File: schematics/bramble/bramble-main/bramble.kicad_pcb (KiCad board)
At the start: 2 copper layers, 50.1 x 72.3 mm, 74 parts, among them IC1 RP2040_QFN56, J1 Conn_01x05_Pin, J2 Conn_01x03, J3 USB_C_Receptacle_USB2.0_16P, J5 U.FL, J6 Conn_01x03_Pin, J7 Conn_02x06_Odd_Even, Q1 DMN3300U, SW1 STM_RESET, SW2 BOOT, SW4 RESET, U1 TDN_5-0910WISM, U2 Opamp_Quad, U3 STM32L031F6P6TR, U4 RFM95W-915S2, U5 MCP1700x-120xxMB, U6 MT25QL01GBBB8ESF-0SIT, U7 W25Q16JVSS, Y1 Crystal, Y3 Crystal

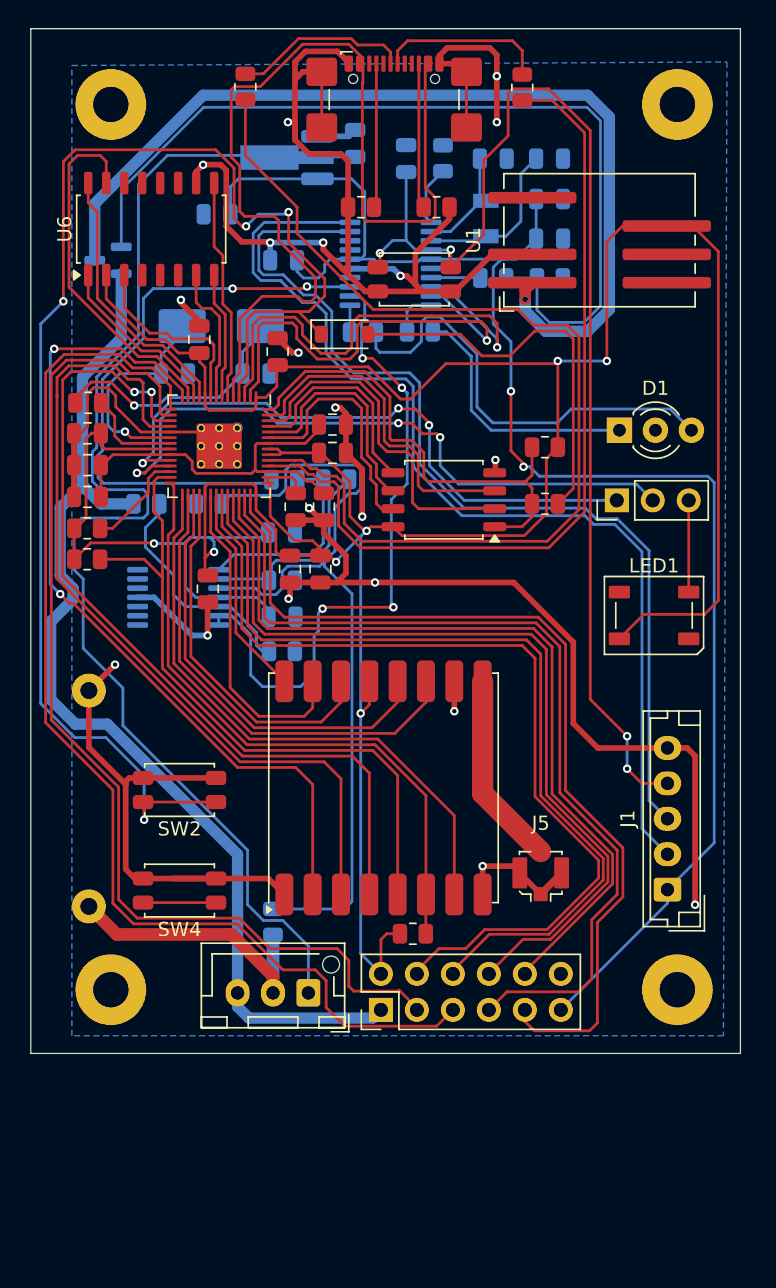
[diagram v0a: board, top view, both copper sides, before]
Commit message: fix: swap spi pins, change footprints, etc
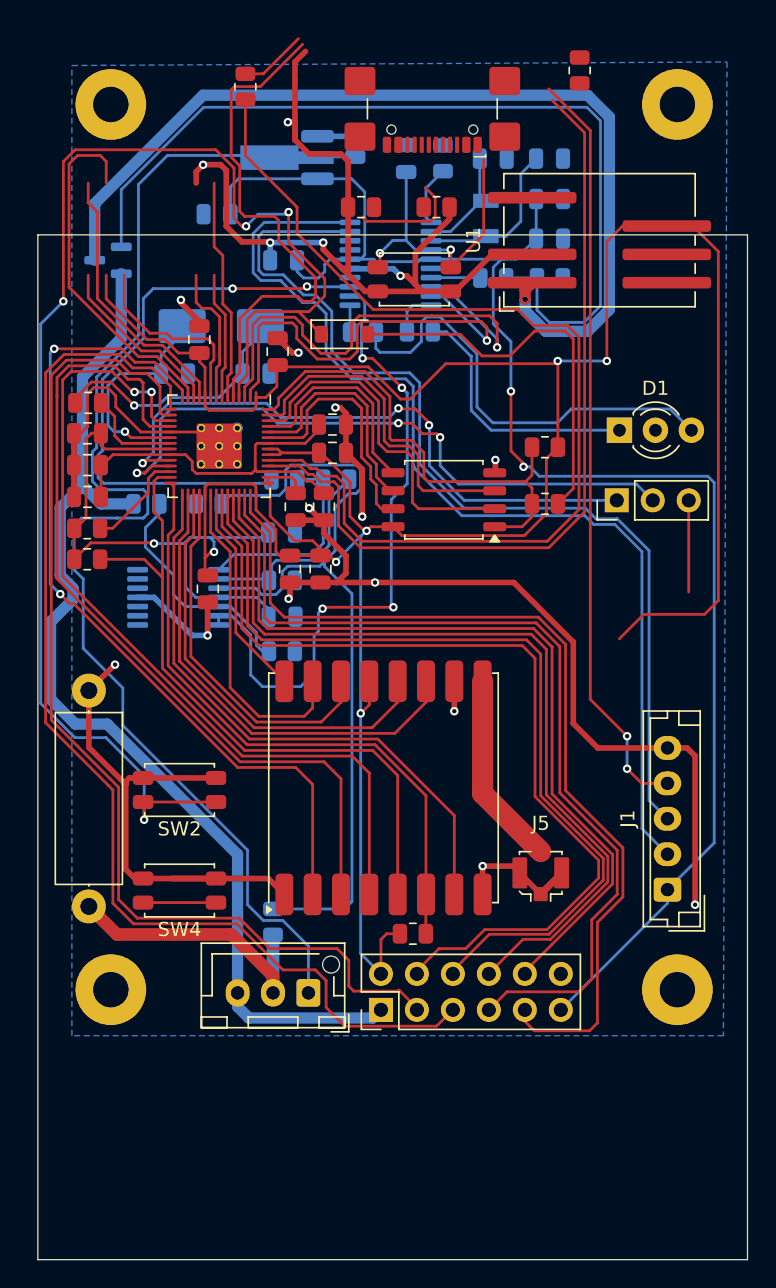
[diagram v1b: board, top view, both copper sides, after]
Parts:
- removed LED1: WS2812B_SK6805_1515, LED_SMD:LED_WS2812B_PLCC4_5.0x5.0mm_P3.2mm
- removed U6: MT25QL01GBBB8ESF-0SIT, Package_SO:SOP-16_4.55x10.3mm_P1.27mm
- R6: moved to F.Cu
- moved R18 4.22 mm to (49.9, 14.6)
- moved J3 3.15 mm to (39.5, 16.2), turned to 180 degrees
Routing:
- net GND: track 249.7 -> 224.8 mm, vias 20 -> 18
- net VBUS: track 69.2 -> 44.5 mm
- net Net-(J3-D--PadA7): track 12.0 -> 0.00 mm
- net Net-(J3-CC1): track 10.2 -> 0.25 mm
- net Net-(J3-CC2): track 10.3 -> 0.48 mm
- net /pmu/NRST: track 83.3 -> 74.9 mm
- net Net-(J3-D+-PadA6): track 12.5 -> 4.78 mm
- net /rp2040/D+: track 59.5 -> 57.4 mm

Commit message: pre-fab check-in of v2
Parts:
- removed U1: TDN_5-0910WISM, Converter_DCDC:Converter_DCDC_TRACO_TDN_5-xxxxWISM_SMD
- added Q2: FDN360P, Package_TO_SOT_SMD:SOT-23, F.Cu at (53.5, 21.4)
- added R3: 100k, Capacitor_SMD:C_0805_2012Metric, F.Cu at (53.4, 26.9)
- added R4: 10k, Capacitor_SMD:C_0805_2012Metric, F.Cu at (53.4, 24.4)
- added RPI_STATUS: WS2812B_SK6805_1515, LED_SMD:LED_WS2812B-2020_PLCC4_2.0x2.0mm, F.Cu at (24.2, 16.8)
- added U7: MT25QL01GBBB8ESF-0SIT, Package_SO:SOIC-16W-12_7.5x10.3mm_P1.27mm, F.Cu at (19.1, 26.2)
- added VR1: TPSM861253RDXR, Bramble:VREG_TPSM861253RDXR, F.Cu at (58.0, 28.2)
- C10: renamed from C8; value 22pF -> 8pF
- C11: renamed from C9; value 22pF -> 8pF
- Q1, R1, R2: moved to F.Cu
- TPS_C_OUT1: renamed from C1; value 10uF -> 22uF
- moved Q1 37.1 mm to (53.2, 33.6), turned to -90 degrees
- moved R2 10.5 mm to (58.0, 31.6)
- moved R1 9.61 mm to (53.4, 29.6)
- moved R24 6.18 mm to (40.5, 23.2), turned to 90 degrees
- moved R21 4.79 mm to (31.0, 15.2)
- moved R23 2.30 mm to (37.7, 23.2), turned to 90 degrees
- moved C21 0.81 mm to (22.2, 33.7)
- renumbered SW2 to BOOT, C3 to C1, C10 to C12, C11 to C13, C12 to C14, C13 to C16, C14 to C17, C15 to C18, C16 to C19, C4 to C2, C17 to C20, C18 to C21, C19 to C22, C20 to C23, C5 to C3, C24 to C4, C23 to C5, C21 to C7, C22 to C8, C7 to C9, D3 to D2, J6 to J2, J2 to J3, J3 to J4, J7 to J6, J1 to PMU_DEBUG, D1 to PMU_STATUS, R8 to R10, R9 to R11, R10 to R12, R22 to R13, R23 to R14, R11 to R15, R12 to R16, R13 to R17, R14 to R18, R15 to R19, R16 to R20, R17 to R21, R18 to R22, R19 to R23, R20 to R24, R21 to R25, R3 to R5, R4 to R6, R5 to R7, R6 to R8, R7 to R9, SW4 to RESET, C2 to TPS_C_IN1, U5 to U4, U4 to U5, U7 to U6, Y3 to Y2
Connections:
- IC1 pad 11: /rp2040/MT25_SCK -> /rp2040/MISO
- IC1 pad 12: /rp2040/MT25_DQ3 -> unconnected-(IC1-GPIO9-Pad12)
- IC1 pad 13: /rp2040/MT25_DQ0 -> unconnected-(IC1-GPIO10-Pad13)
- IC1 pad 14: /rp2040/MISO -> unconnected-(IC1-GPIO11-Pad14)
- IC1 pad 54: /rp2040/QSPI_D1 -> /rp2040/QSPI_D2
- IC1 pad 55: /rp2040/QSPI_D2 -> /rp2040/QSPI_D1
- IC1 pad 6: /rp2040/MT25_DQ2 -> /rp2040/RGB_LED
- IC1 pad 7: /rp2040/MT25_DQ1 -> unconnected-(IC1-GPIO5-Pad7)
- Q1 pad 2: +9V -> GND
- RESET pad 1: unconnected-(SW4-Pad1) -> /rp2040/~{RESET}
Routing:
- net Net-(Q1-D): track 67.1 -> 8.21 mm, vias 1 -> 0
- net Net-(Q1-G): track 63.5 -> 6.18 mm
- net +9V: track 76.2 -> 131.8 mm, vias 0 -> 1
- net /pmu/3V3_POWER_ON: track 3.52 -> 43.1 mm, vias 0 -> 1
- net /rp2040/~{RESET}: track 7.21 -> 42.4 mm, vias 0 -> 2
- net GND: track 224.8 -> 259.2 mm, vias 18 -> 19
- net /rp2040/MT25_DQ0: track 25.3 -> 0.00 mm
- net /rp2040/RGB_LED: track 0.00 -> 23.9 mm
- net /rp2040/SCK: track 60.1 -> 80.4 mm, vias 2 -> 3
- net /rp2040/MT25_SCK: track 19.1 -> 0.00 mm
- net /rp2040/MOSI: track 59.9 -> 78.7 mm, vias 0 -> 2
- net /pmu/NRST: track 74.9 -> 93.2 mm, vias 4 -> 3
- net /rp2040/MISO: track 59.7 -> 76.8 mm
- net Net-(J4-D--PadA7): track 0.00 -> 16.7 mm, vias 0 -> 2
- net /rp2040/MT25_DQ2: track 15.7 -> 0.00 mm
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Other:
- board size 50.1 x 72.3 mm -> 50.4 x 70.7 mm
- board text added: "Bramble v0.2 Erik E. Beerepoot"
- board text added: "RPI_SWD"
- board text added: "⏚"

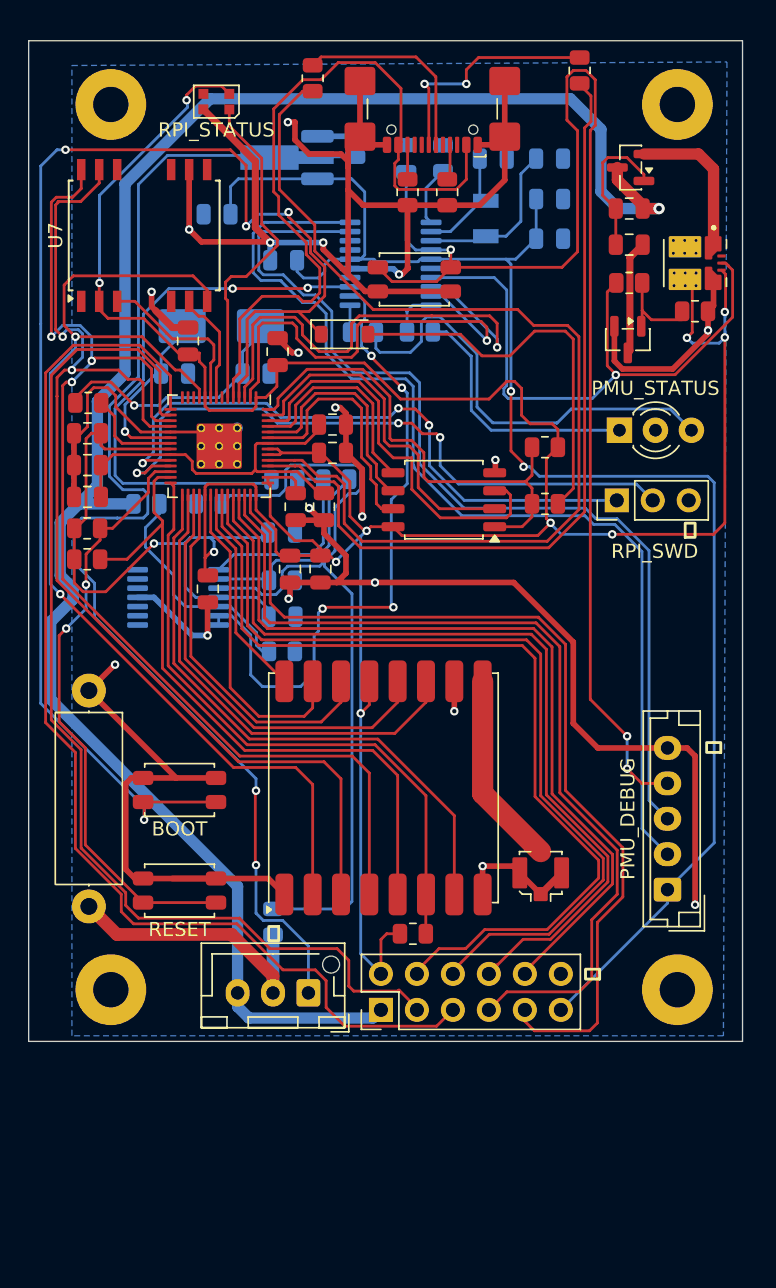
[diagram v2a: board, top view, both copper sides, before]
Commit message: v3: add art, reposition pin headers and ufl connector
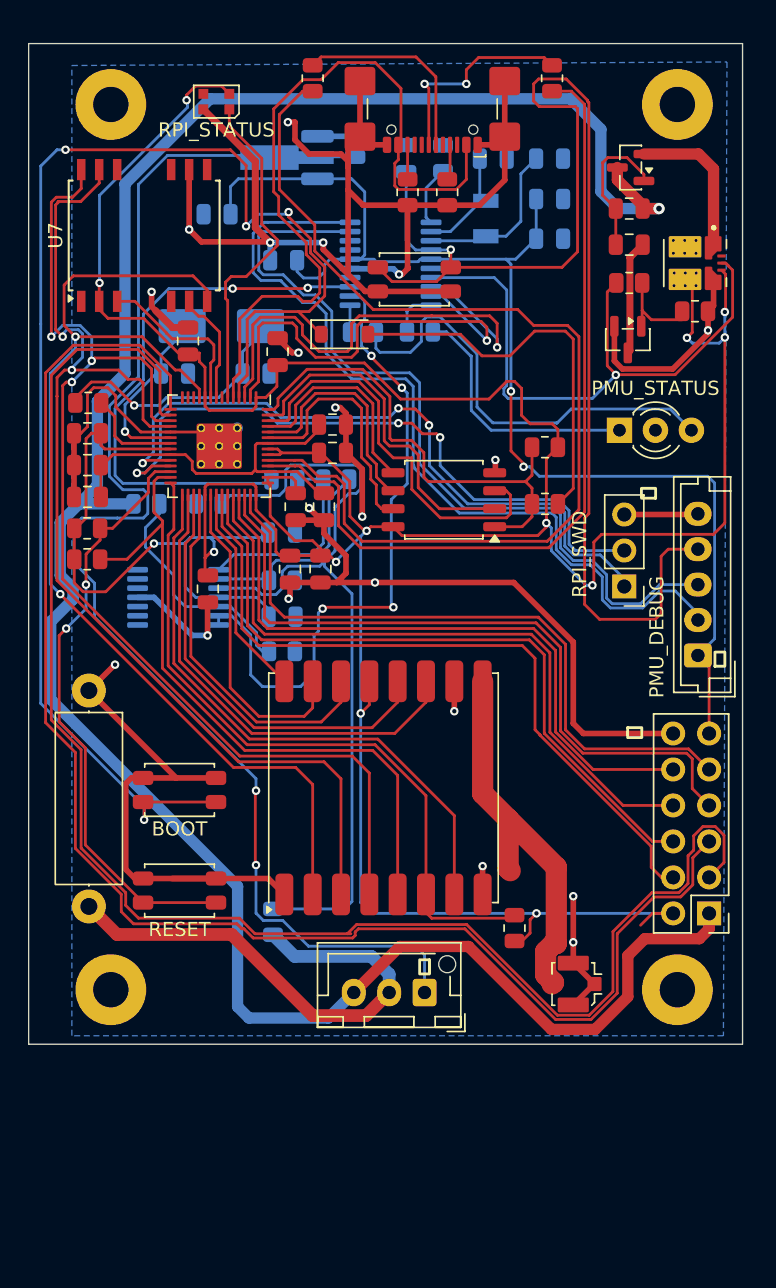
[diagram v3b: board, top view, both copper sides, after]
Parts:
- added G***: LOGO, Bramble:bramble logo, B.Cu at (44.9, 61.9)
- moved J6 24.2 mm to (59.0, 74.1), turned to 180 degrees
- moved PMU_DEBUG 16.7 mm to (58.2, 55.9)
- moved J2 8.20 mm to (38.9, 79.7)
- moved J5 8.18 mm to (49.4, 79.1), turned to -90 degrees
- moved R19 7.19 mm to (45.2, 75.2), turned to -90 degrees
- moved J3 6.10 mm to (53.0, 51.0), turned to 180 degrees
- moved R22 2.03 mm to (47.9, 15.2)
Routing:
- net /rp2040/VALVE_3: track 77.1 -> 112.0 mm
- net +9V: track 131.8 -> 165.0 mm
- net /rp2040/VALVE_4: track 81.5 -> 107.3 mm
- net +3V3: track 253.9 -> 277.9 mm, vias 12 -> 13
- net VDD: track 111.5 -> 88.3 mm
- net /rp2040/VALVE_1: track 66.7 -> 47.6 mm
- net /rp2040/VALVE_2: track 66.3 -> 50.8 mm
- net GNDPWR: track 20.3 -> 35.7 mm
- net Net-(J5-In): track 13.7 -> 27.9 mm
- net Net-(J1-Pin_2): track 72.7 -> 60.0 mm
- net /rp2040/MOTOR_HI_2: track 61.8 -> 49.4 mm
- net /rp2040/MOTOR_HI_1: track 63.9 -> 51.6 mm
- net /rp2040/MOTOR_LO_1: track 59.7 -> 47.9 mm
- net Net-(J1-Pin_3): track 69.2 -> 57.6 mm
- net /rp2040/MOTOR_LO_2: track 57.6 -> 46.4 mm
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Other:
- board size 50.4 x 70.7 mm -> 50.4 x 70.6 mm
- board text added: "BRAMBLE"
- board text added: "PWR"
- board text added: "v0.3 E. E. Beerepoot"
- board text removed: "Bramble v0.2 Erik E. Beerepoot"

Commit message: v3 of schematic
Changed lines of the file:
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@@
 	)
 	(segment
-		(start 47.85 48.502712)
-		(end 47.85 46.9)
-		(width 0.2)
-		(layer "B.Cu")
-		(net 7)
-	)
-	(segment
 		(start 19.796 48)
 		(end 21.93 48)
@@
 	)
 	(segment
-		(start 59.7 33.85)
-		(end 60.1 33.45)
+		(start 50.402 49.802)
+		(end 49.149288 49.802)
 		(width 0.2)
 		(layer "B.Cu")
@@
 	)
 	(segment
-		(start 60.1 31.65)
+		(start 59.7 33.85)
 		(end 60.1 33.45)
 		(width 0.2)
@@
 	)
 	(segment
-		(start 50.75 50.95)
-		(end 50.297288 50.95)
+		(start 60.1 31.65)
+		(end 60.1 33.45)
 		(width 0.2)
 		(layer "B.Cu")
@@
 	)
 	(segment
+		(start 47.85 47.25)
+		(end 47.85 46.9)
+		(width 0.2)
+		(layer "B.Cu")
+		(net 7)
+	)
+	(segment
+		(start 47.896 48.548712)
+		(end 47.896 47.296)
+		(width 0.2)
+		(layer "B.Cu")
+		(net 7)
+	)
+	(segment
 		(start 34.39 59.99)
 		(end 34.39 73.35)
@@
 	)
 	(segment
+		(start 50.75 50.95)
+		(end 50.75 50.15)
+		(width 0.2)
+		(layer "B.Cu")
+		(net 7)
+	)
+	(segment
 		(start 22.355 47.575)
 		(end 22.01 47.92)
@@
 	)
 	(segment
+		(start 50.75 50.15)
+		(end 50.402 49.802)
+		(width 0.2)
+		(layer "B.Cu")
+		(net 7)
+	)
+	(segment
 		(start 57.8 33.85)
 		(end 59.7 33.85)
@@
 	)
 	(segment
+		(start 49.149288 49.802)
+		(end 47.896 48.548712)
+		(width 0.2)
+		(layer "B.Cu")
+		(net 7)
+	)
+	(segment
 		(start 23.75 47.575)
 		(end 22.355 47.575)
@@
 	)
 	(segment
-		(start 22.01 51.07)
-		(end 22.01 47.92)
+		(start 47.896 47.296)
+		(end 47.85 47.25)
 		(width 0.2)
 		(layer "B.Cu")
@@
 	)
 	(segment
-		(start 34.39 47.49)
-		(end 34.776776 47.103224)
+		(start 22.01 51.07)
+		(end 22.01 47.92)
 		(width 0.2)
 		(layer "B.Cu")
@@
 	)
 	(segment
-		(start 50.297288 50.95)
-		(end 47.85 48.502712)
+		(start 34.39 47.49)
+		(end 34.776776 47.103224)
 		(width 0.2)
 		(layer "B.Cu")
@@
 	)
 	(segment
-		(start 40 42.5)
-		(end 42.398 44.898)
+		(start 48.323678 44.898)
+		(end 49.1 45.674322)
 		(width 0.2)
 		(layer "B.Cu")
@@
 	)
 	(segment
-		(start 19.154375 43.017044)
-		(end 18.59513 43.017044)
+		(start 40 40.5)
+		(end 40 42.5)
 		(width 0.2)
 		(layer "B.Cu")
@@
 	)
 	(segment
-		(start 51.83 48.5)
-		(end 51.84 48.49)
+		(start 19.154375 43.017044)
+		(end 18.59513 43.017044)
 		(width 0.2)
 		(layer "B.Cu")
@@
 	)
 	(segment
-		(start 49.1 48.05)
-		(end 49.55 48.5)
+		(start 42.398 44.898)
+		(end 48.323678 44.898)
 		(width 0.2)
 		(layer "B.Cu")
@@
 	)
 	(segment
-		(start 51.84 48.49)
-		(end 53 48.49)
-		(width 0.2)
-		(layer "B.Cu")
-		(net 10)
-	)
-	(segment
-		(start 42.398 44.898)
-		(end 48.323678 44.898)
-		(width 0.2)
-		(layer "B.Cu")
-		(net 10)
-	)
-	(segment
-		(start 40 40.5)
-		(end 40 42.5)
+		(start 49.1 48)
+		(end 49.59 48.49)
 		(width 0.2)
 		(layer "B.Cu")
@@
 	(segment
 		(start 49.1 45.674322)
-		(end 49.1 48.05)
+		(end 49.1 48)
 		(width 0.2)
 		(layer "B.Cu")
@@
 	)
 	(segment
-		(start 49.55 48.5)
-		(end 51.83 48.5)
+		(start 37.054 39.5)
+		(end 28.5 39.5)
 		(width 0.2)
 		(layer "B.Cu")
@@
 	)
 	(segment
-		(start 37.054 39.5)
-		(end 28.5 39.5)
+		(start 40 42.5)
+		(end 42.398 44.898)
 		(width 0.2)
 		(layer "B.Cu")
@@
 	)
 	(segment
-		(start 20.25 39.25)
-		(end 20.25 41.921419)
+		(start 49.59 48.49)
+		(end 53 48.49)
 		(width 0.2)
 		(layer "B.Cu")
@@
 	)
 	(segment
-		(start 48.323678 44.898)
-		(end 49.1 45.674322)
+		(start 20.25 39.25)
+		(end 20.25 41.921419)
 		(width 0.2)
 		(layer "B.Cu")
@@
 	)
 	(segment
-		(start 31.199 30.451)
-		(end 31.2 30.45)
+		(start 28.926 29.026)
+		(end 30.351 30.451)
 		(width 0.2)
 		(layer "B.Cu")
@@
 	)
 	(segment
-		(start 55.5 50.9)
-		(end 58.2 50.9)
+		(start 33.9 35.95)
+		(end 37.85 35.95)
 		(width 0.2)
 		(layer "B.Cu")
@@
 	)
 	(segment
-		(start 49.398644 49.2)
-		(end 50.75 49.2)
+		(start 27.199 28.71016)
+		(end 27.51484 29.026)
 		(width 0.2)
 		(layer "B.Cu")
@@
 	)
 	(segment
-		(start 27.51484 29.026)
-		(end 28.926 29.026)
+		(start 30.351 30.451)
+		(end 31.199 30.451)
 		(width 0.2)
 		(layer "B.Cu")
@@
 	)
 	(segment
-		(start 48.05 45.5)
-		(end 48.498 45.948)
+		(start 33.6375 25.975)
+		(end 27.5 25.975)
 		(width 0.2)
 		(layer "B.Cu")
@@
 	)
 	(segment
-		(start 31.2 30.45)
-		(end 32.35 31.6)
+		(start 32.35 34.4)
+		(end 33.9 35.95)
 		(width 0.2)
 		(layer "B.Cu")
@@
 	)
 	(segment
-		(start 37.85 35.95)
-		(end 38.55 36.65)
+		(start 27.51484 29.026)
+		(end 28.926 29.026)
 		(width 0.2)
 		(layer "B.Cu")
@@
 	)
 	(segment
-		(start 33.6375 25.975)
-		(end 27.5 25.975)
+		(start 54.15 52.25)
+		(end 55.5 50.9)
 		(width 0.2)
 		(layer "B.Cu")
@@
 	)
 	(segment
-		(start 32.35 31.6)
-		(end 32.35 34.4)
+		(start 27.199 26.276)
+		(end 27.199 28.71016)
 		(width 0.2)
 		(layer "B.Cu")
@@
 	)
 	(segment
-		(start 51.75 51.85)
-		(end 52.15 52.25)
+		(start 31.199 30.451)
+		(end 31.2 30.45)
 		(width 0.2)
 		(layer "B.Cu")
@@
 	)
 	(segment
-		(start 38.55 36.65)
-		(end 38.55 42.3671)
+		(start 48.498 45.948)
+		(end 48.498 48.299356)
 		(width 0.2)
 		(layer "B.Cu")
@@
 	)
 	(segment
-		(start 48.498 45.948)
-		(end 48.498 48.299356)
+		(start 37.85 35.95)
+		(end 38.55 36.65)
 		(width 0.2)
 		(layer "B.Cu")
@@
 	)
 	(segment
-		(start 28.926 29.026)
-		(end 30.351 30.451)
+		(start 38.55 36.65)
+		(end 38.55 42.3671)
 		(width 0.2)
 		(layer "B.Cu")
@@
 	)
 	(segment
-		(start 30.351 30.451)
-		(end 31.199 30.451)
+		(start 55.5 50.9)
+		(end 58.2 50.9)
 		(width 0.2)
 		(layer "B.Cu")
@@
 	)
 	(segment
-		(start 41.6829 45.5)
-		(end 48.05 45.5)
+		(start 48.05 45.5)
+		(end 48.498 45.948)
 		(width 0.2)
 		(layer "B.Cu")
@@
 	)
 	(segment
-		(start 27.199 28.71016)
-		(end 27.51484 29.026)
+		(start 50.9 49.2)
+		(end 51.75 50.05)
 		(width 0.2)
 		(layer "B.Cu")
@@
 	)
 	(segment
-		(start 27.199 26.276)
-		(end 27.199 28.71016)
+		(start 32.35 31.6)
+		(end 32.35 34.4)
 		(width 0.2)
 		(layer "B.Cu")
@@
 	)
 	(segment
-		(start 27.5 25.975)
-		(end 27.199 26.276)
+		(start 38.55 42.3671)
+		(end 41.6829 45.5)
 		(width 0.2)
 		(layer "B.Cu")
@@
 	)
 	(segment
-		(start 38.55 42.3671)
-		(end 41.6829 45.5)
+		(start 41.6829 45.5)
+		(end 48.05 45.5)
 		(width 0.2)
 		(layer "B.Cu")
@@
 	)
 	(segment
-		(start 33.9 35.95)
-		(end 37.85 35.95)
+		(start 51.75 51.85)
+		(end 52.15 52.25)
 		(width 0.2)
 		(layer "B.Cu")
@@
 	)
 	(segment
-		(start 51.75 50.2)
-		(end 51.75 51.85)
+		(start 31.2 30.45)
+		(end 32.35 31.6)
 		(width 0.2)
 		(layer "B.Cu")
@@
 	)
 	(segment
-		(start 54.15 52.25)
-		(end 55.5 50.9)
+		(start 51.75 50.05)
+		(end 51.75 51.85)
 		(width 0.2)
 		(layer "B.Cu")
@@
 	)
 	(segment
-		(start 32.35 34.4)
-		(end 33.9 35.95)
+		(start 49.398644 49.2)
+		(end 50.9 49.2)
 		(width 0.2)
 		(layer "B.Cu")
@@
 	)
 	(segment
-		(start 50.75 49.2)
-		(end 51.75 50.2)
+		(start 27.5 25.975)
+		(end 27.199 26.276)
 		(width 0.2)
 		(layer "B.Cu")

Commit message: Check in some of the v3 change
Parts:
- removed RPI_STATUS: WS2812B_SK6805_1515, LED_SMD:LED_WS2812B-2020_PLCC4_2.0x2.0mm
- added RPI_STATUS1: WS2812B-2020, LED_SMD:LED_WS2812B-2020_PLCC4_2.0x2.0mm, F.Cu at (24.2, 16.8)
- moved R14 0.15 mm to (34.7, 33.0)
- renumbered C16 to C15, C17 to C16, C18 to C17, C19 to C18, C20 to C19, C21 to C20, C22 to C21, C23 to C22, PMU_STATUS to D1, PMU_DEBUG to J1, BOOT to SW2, RESET to SW3, U2 to U1, U3 to U2, U4 to U3, U5 to U4, U6 to U5, U7 to U6
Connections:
- VR1 pad 5: +3V3 -> unconnected-(VR1-PG-Pad5)
- VR1 pad 7: unconnected-(VR1-VOS-Pad7) -> +3V3
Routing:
- net Net-(J5-In): track 27.9 -> 24.2 mm
- net +3V3: track 278.4 -> 277.4 mm, vias 13 -> 12
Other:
- board text added: "GPIO"
- board text added: "RESET"
- board text added: "RPI STATUS"
- board text added: "RPI SWD"
- board text added: "STM DEBUG"
- board text added: "STM RESET"
- board text added: "STM STATUS"
- board text added: "v0.4, Dec 2025 E. E. Beerepoot"
- board text removed: "v0.3 E. E. Beerepoot"
